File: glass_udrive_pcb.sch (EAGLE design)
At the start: 14 parts, among them IC1 OPA129U, J1 OMNETICS_A75243-001

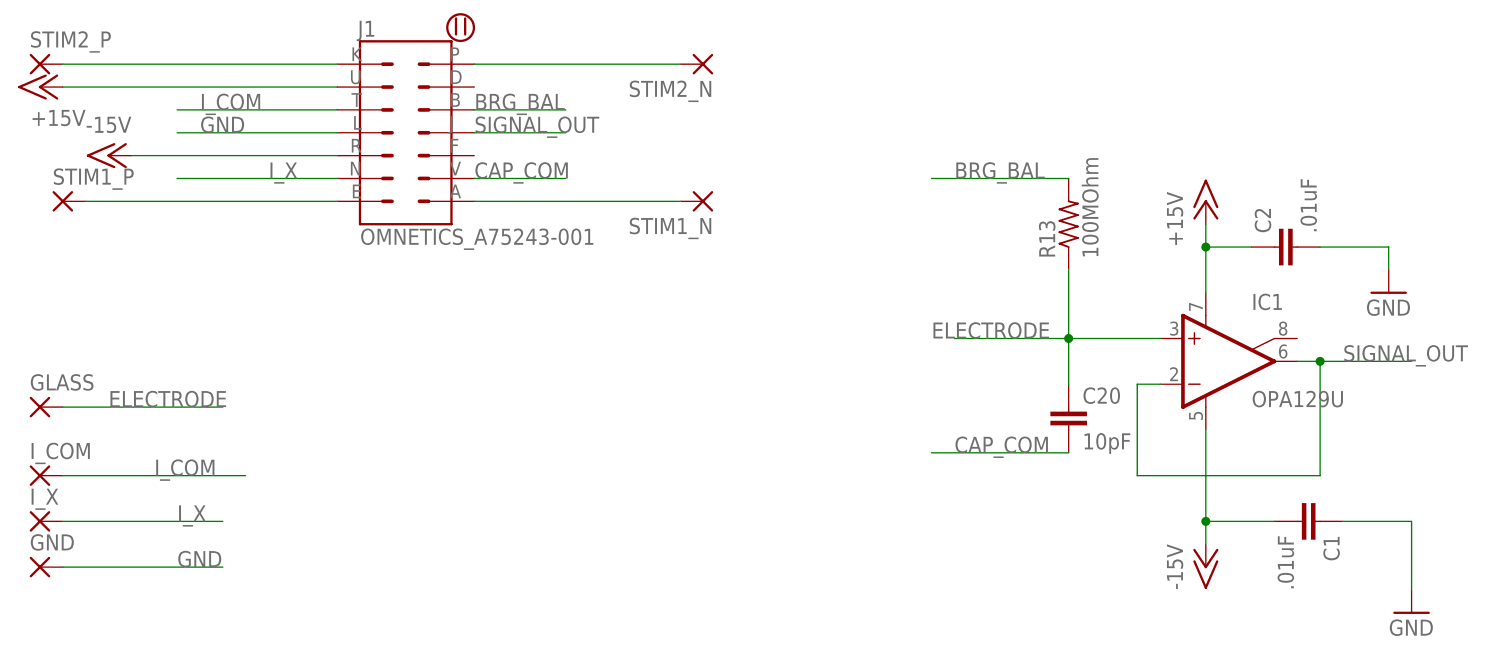
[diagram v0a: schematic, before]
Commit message: smashed labels
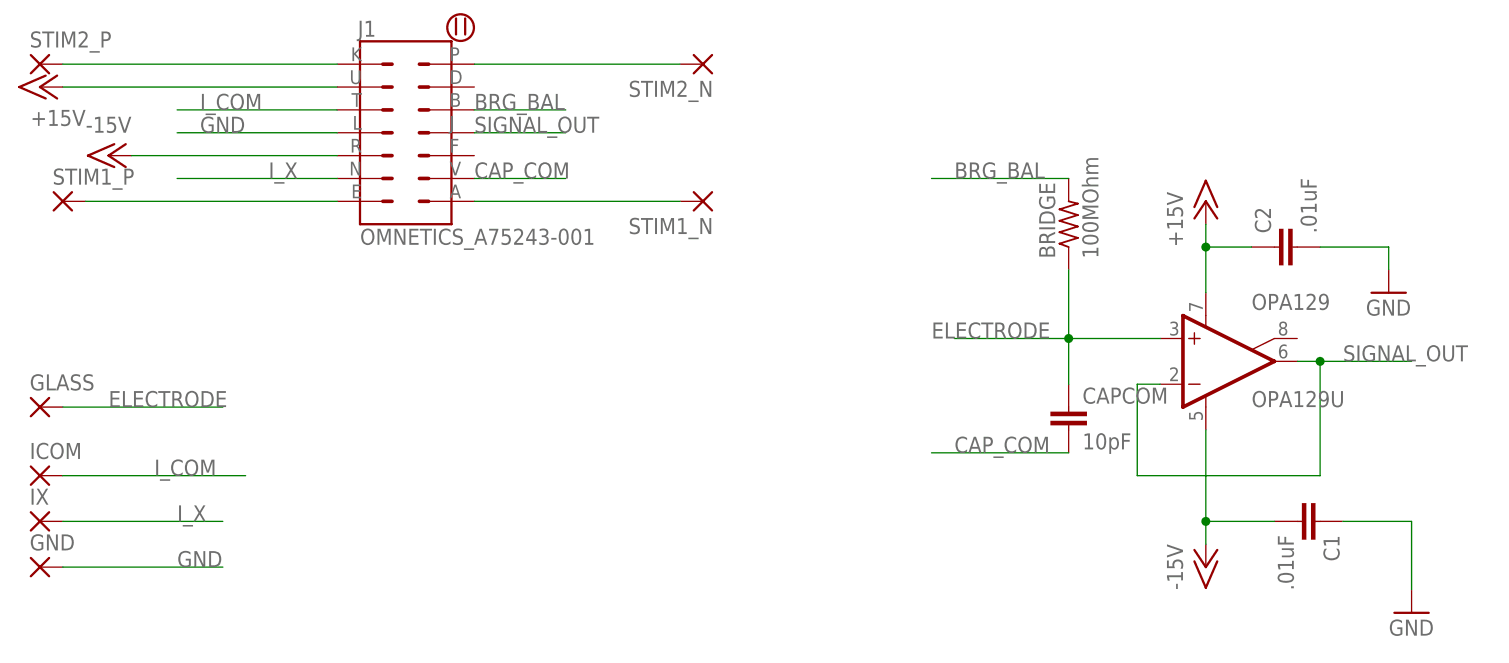
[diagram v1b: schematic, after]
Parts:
- renumbered C20 to CAPCOM, IC1 to OPA129, I_COM to ICOM, I_X to IX, R13 to BRIDGE
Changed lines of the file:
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@@
 </classes>
 <parts>
-<part name="IC1" library="burr-brown" deviceset="OPA129" device="U"/>
+<part name="OPA129" library="burr-brown" deviceset="OPA129" device="U"/>
 <part name="FRAME1" library="frames" deviceset="LETTER_L" device=""/>
 <part name="J1" library="GFL" deviceset="OMNETICS_A75243-001" device=""/>
-<part name="R13" library="GFL" deviceset="R" device="_0402" value="100MOhm"/>
-<part name="C20" library="GFL" deviceset="C" device="_0402" value="10pF"/>
+<part name="BRIDGE" library="GFL" deviceset="R" device="_0402" value="100MOhm"/>
+<part name="CAPCOM" library="GFL" deviceset="C" device="_0402" value="10pF"/>
 <part name="C1" library="GFL" deviceset="C" device="_0402" value=".01uF"/>
 <part name="C2" library="GFL" deviceset="C" device="_0402" value=".01uF"/>
@@
 <part name="GLASS" library="GFL" deviceset="THROUGH-HOLE-30MIL/15MIL" device=""/>
 <part name="STIM2_N" library="GFL" deviceset="THROUGH-HOLE-30MIL/15MIL" device=""/>
-<part name="I_X" library="GFL" deviceset="THROUGH-HOLE-30MIL/15MIL" device=""/>
+<part name="IX" library="GFL" deviceset="THROUGH-HOLE-30MIL/15MIL" device=""/>
 <part name="STIM1_N" library="GFL" deviceset="THROUGH-HOLE-30MIL/15MIL" device=""/>
 <part name="STIM1_P" library="GFL" deviceset="THROUGH-HOLE-30MIL/15MIL" device=""/>
 <part name="STIM2_P" library="GFL" deviceset="THROUGH-HOLE-30MIL/15MIL" device=""/>
-<part name="I_COM" library="GFL" deviceset="THROUGH-HOLE-30MIL/15MIL" device=""/>
+<part name="ICOM" library="GFL" deviceset="THROUGH-HOLE-30MIL/15MIL" device=""/>
 <part name="GND" library="GFL" deviceset="THROUGH-HOLE-30MIL/15MIL" device=""/>
 </parts>
@@
 </plain>
 <instances>
-<instance part="IC1" gate="G$1" x="149.86" y="91.44"/>
+<instance part="OPA129" gate="G$1" x="149.86" y="91.44"/>
 <instance part="FRAME1" gate="G$1" x="-25.4" y="-10.16"/>
 <instance part="FRAME1" gate="G$2" x="121.92" y="-10.16"/>
 <instance part="J1" gate="G$1" x="58.42" y="116.84"/>
-<instance part="R13" gate="R" x="132.08" y="106.68" rot="R90"/>
-<instance part="C20" gate="C" x="132.08" y="86.36"/>
+<instance part="BRIDGE" gate="R" x="132.08" y="106.68" rot="R90"/>
+<instance part="CAPCOM" gate="C" x="132.08" y="86.36"/>
 <instance part="C1" gate="C" x="160.02" y="73.66" rot="R270"/>
 <instance part="C2" gate="C" x="154.94" y="104.14" rot="R90"/>
@@
 <instance part="GLASS" gate="P" x="17.78" y="86.36"/>
 <instance part="STIM2_N" gate="P" x="91.44" y="124.46" rot="R180"/>
-<instance part="I_X" gate="P" x="17.78" y="73.66"/>
+<instance part="IX" gate="P" x="17.78" y="73.66"/>
 <instance part="STIM1_N" gate="P" x="91.44" y="109.22" rot="R180"/>
 <instance part="STIM1_P" gate="P" x="20.32" y="109.22"/>
 <instance part="STIM2_P" gate="P" x="17.78" y="124.46"/>
-<instance part="I_COM" gate="P" x="17.78" y="78.74"/>
+<instance part="ICOM" gate="P" x="17.78" y="78.74"/>
 <instance part="GND" gate="P" x="17.78" y="68.58"/>
 </instances>
@@
 <net name="+15V" class="0">
 <segment>
-<pinref part="IC1" gate="G$1" pin="V+"/>
+<pinref part="OPA129" gate="G$1" pin="V+"/>
 <pinref part="P+1" gate="1" pin="+15V"/>
 <wire x1="147.32" y1="106.68" x2="147.32" y2="104.14" width="0.1524" layer="91"/>
@@
 <net name="-15V" class="0">
 <segment>
-<pinref part="IC1" gate="G$1" pin="V-"/>
+<pinref part="OPA129" gate="G$1" pin="V-"/>
 <pinref part="P-1" gate="1" pin="-15V"/>
 <wire x1="147.32" y1="71.12" x2="147.32" y2="73.66" width="0.1524" layer="91"/>
@@
 <net name="ELECTRODE" class="0">
 <segment>
-<pinref part="IC1" gate="G$1" pin="+IN"/>
+<pinref part="OPA129" gate="G$1" pin="+IN"/>
 <wire x1="142.24" y1="93.98" x2="132.08" y2="93.98" width="0.1524" layer="91"/>
-<pinref part="C20" gate="C" pin="1"/>
+<pinref part="CAPCOM" gate="C" pin="1"/>
 <wire x1="132.08" y1="88.9" x2="132.08" y2="93.98" width="0.1524" layer="91"/>
 <junction x="132.08" y="93.98"/>
-<pinref part="R13" gate="R" pin="1"/>
+<pinref part="BRIDGE" gate="R" pin="1"/>
 <wire x1="132.08" y1="93.98" x2="132.08" y2="101.6" width="0.1524" layer="91"/>
 <wire x1="132.08" y1="93.98" x2="119.38" y2="93.98" width="0.1524" layer="91"/>
@@
 </segment>
 <segment>
-<pinref part="C20" gate="C" pin="2"/>
+<pinref part="CAPCOM" gate="C" pin="2"/>
 <wire x1="132.08" y1="81.28" x2="116.84" y2="81.28" width="0.1524" layer="91"/>
 <label x="119.38" y="81.28" size="1.778" layer="95"/>
@@
 </segment>
 <segment>
-<pinref part="R13" gate="R" pin="2"/>
+<pinref part="BRIDGE" gate="R" pin="2"/>
 <wire x1="132.08" y1="111.76" x2="116.84" y2="111.76" width="0.1524" layer="91"/>
 <label x="119.38" y="111.76" size="1.778" layer="95"/>
@@
 <wire x1="20.32" y1="78.74" x2="40.64" y2="78.74" width="0.1524" layer="91"/>
 <label x="30.48" y="78.74" size="1.778" layer="95"/>
-<pinref part="I_COM" gate="P" pin="P"/>
+<pinref part="ICOM" gate="P" pin="P"/>
 </segment>
 <segment>
@@
 <net name="I_X" class="0">
 <segment>
-<pinref part="I_X" gate="P" pin="P"/>
+<pinref part="IX" gate="P" pin="P"/>
 <wire x1="20.32" y1="73.66" x2="38.1" y2="73.66" width="0.1524" layer="91"/>
 <label x="33.02" y="73.66" size="1.778" layer="95"/>
@@
 </segment>
 <segment>
-<pinref part="IC1" gate="G$1" pin="-IN"/>
+<pinref part="OPA129" gate="G$1" pin="-IN"/>
 <wire x1="142.24" y1="88.9" x2="139.7" y2="88.9" width="0.1524" layer="91"/>
 <wire x1="139.7" y1="88.9" x2="139.7" y2="78.74" width="0.1524" layer="91"/>
 <wire x1="139.7" y1="78.74" x2="160.02" y2="78.74" width="0.1524" layer="91"/>
 <wire x1="160.02" y1="78.74" x2="160.02" y2="91.44" width="0.1524" layer="91"/>
-<pinref part="IC1" gate="G$1" pin="OUT"/>
+<pinref part="OPA129" gate="G$1" pin="OUT"/>
 <wire x1="160.02" y1="91.44" x2="157.48" y2="91.44" width="0.1524" layer="91"/>
 <wire x1="160.02" y1="91.44" x2="170.18" y2="91.44" width="0.1524" layer="91"/>

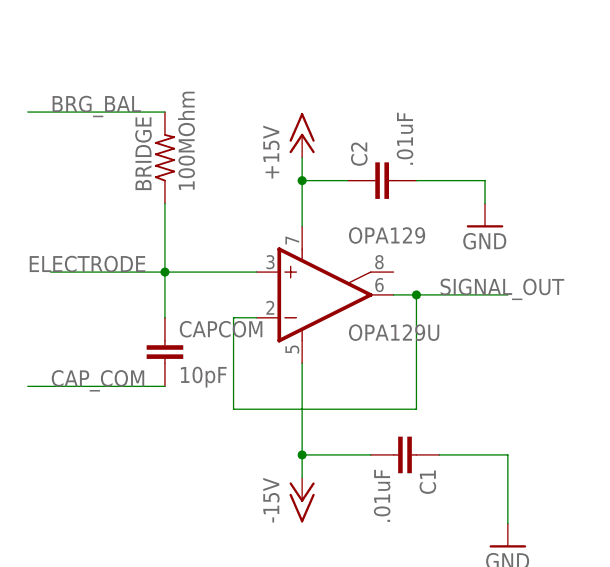
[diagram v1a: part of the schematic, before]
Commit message: Galen's suggested changes to Rev 1.0
I have changed a number of things in your design, one of which is major and the
rest are minor. The major change is that I have added a guard trace to your
design, in accordance with the data sheet for the OPA129. If you are going to
use an ultra-low input bias current op amp, then you should make efforts to
actually achieve the performance that it touts. The other changes are mostly
positioning to accommodate the guard trace, changes to the silk screen on your
board, and simplification of the routing of some traces.

To achieve very low input bias, you need to make sure that there is no leakage
current to the electrode net from the rest of the PCB. There is some parasitic
resistance between neighboring traces in the PCB through the insulator and the
solder-mask. By surrounding the electrode with a copper trace that is driven to
be the same voltage as the electrode, this eliminates parasitic resistance, and
also reduces the stray capacitance of the electrode. I am mainly just following
the recommendations of the data sheet for the OPA129, so for more details see the
data sheet. I moved the bridge resistor and compensation capacitor closer to the
electrode to minimize the length of the electrode trace on your board, since
it's a high impedance trace that should be minimized and protected to avoid
noise pickup. I also placed the cap and res so that the guard trace runs between
the pads. To be honest, with these in place the point of using the OPA129 is
lost on me, since you'll have more parasitic current through these than through
any op amp. However, if you do not place them (which you probably will not need
to), then you will have very little input bias current. Running the trace
through the pads is manufacturable at PCBWay (0.1mm minimum), but may cost more.
I think the difference in cost will be totally worth it. We're not that price
sensitive. I also added a break in the solder mask for the guard traces, once
again to minimize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
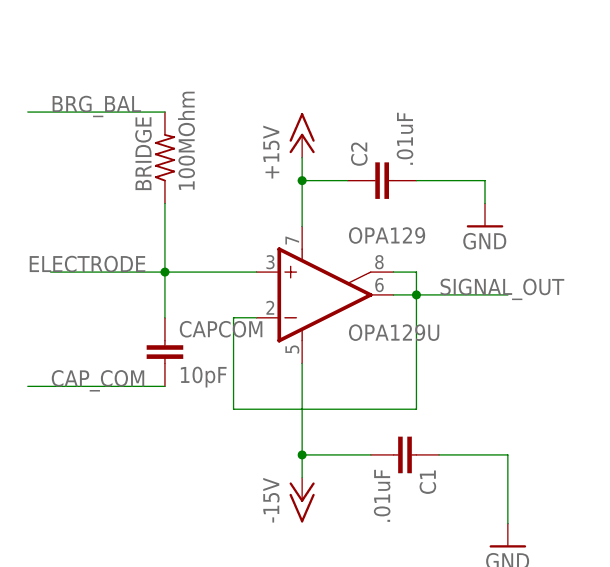
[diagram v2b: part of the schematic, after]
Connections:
- net SIGNAL_OUT: now also OPA129.SUBS
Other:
- note added: "1.0"
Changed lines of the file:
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@@
 <sheet>
 <plain>
+<text x="213.36" y="-2.54" size="1.778" layer="101">1.0</text>
 </plain>
 <instances>
@@
 <junction x="160.02" y="91.44"/>
 <label x="162.56" y="91.44" size="1.778" layer="95"/>
+<pinref part="OPA129" gate="G$1" pin="SUBS"/>
+<wire x1="157.48" y1="93.98" x2="160.02" y2="93.98" width="0.1524" layer="91"/>
+<wire x1="160.02" y1="93.98" x2="160.02" y2="91.44" width="0.1524" layer="91"/>
 </segment>
 </net>
@@
 </sheet>
 </sheets>
+<errors>
+</errors>
 </schematic>
 </drawing>

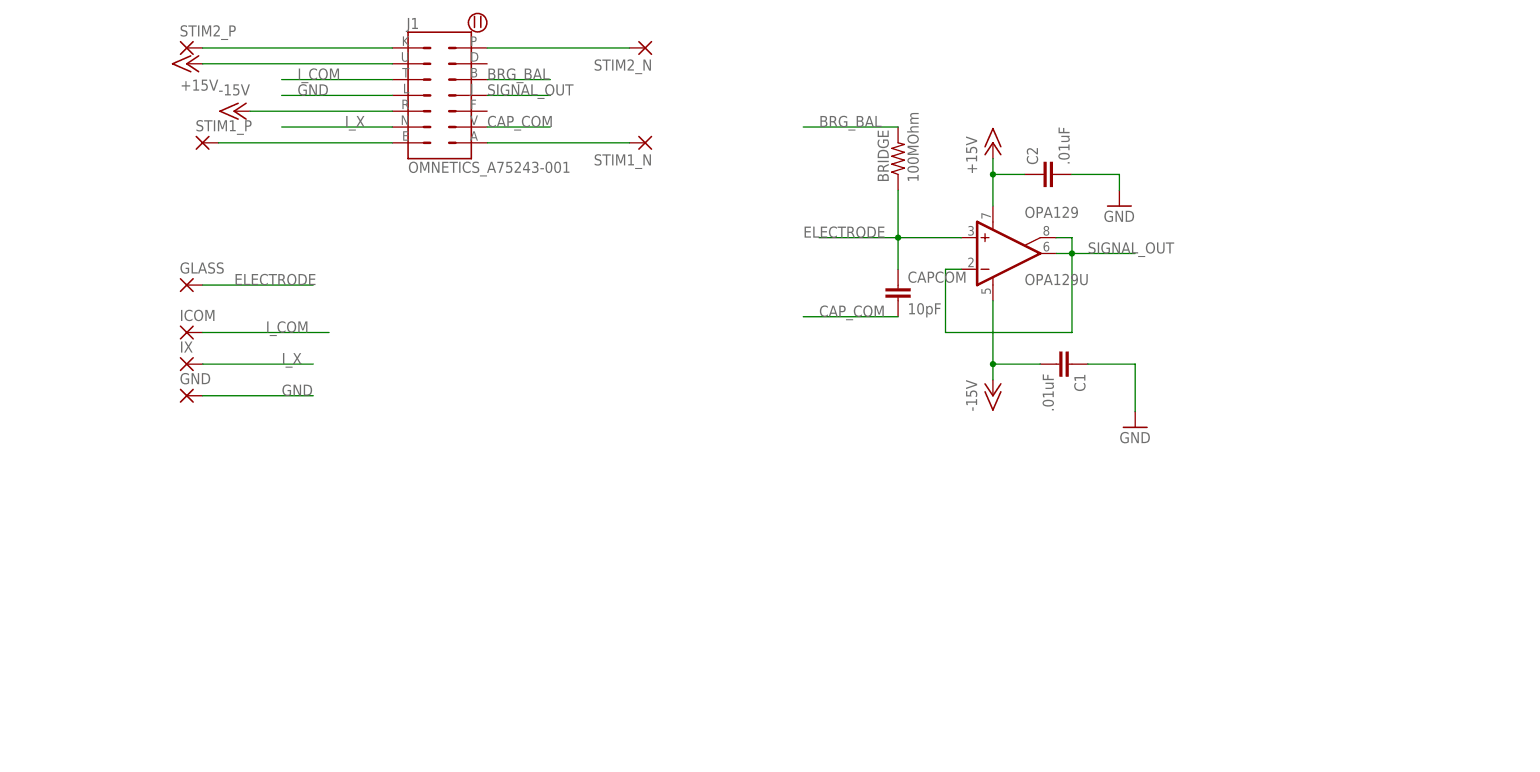
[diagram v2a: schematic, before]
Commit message: Revision AD8224 redesigned to use instrumentation amplifier with a reference electrode. This version has 2 input and 2 INA output channels one for glass electrode and another for a metal electrode.
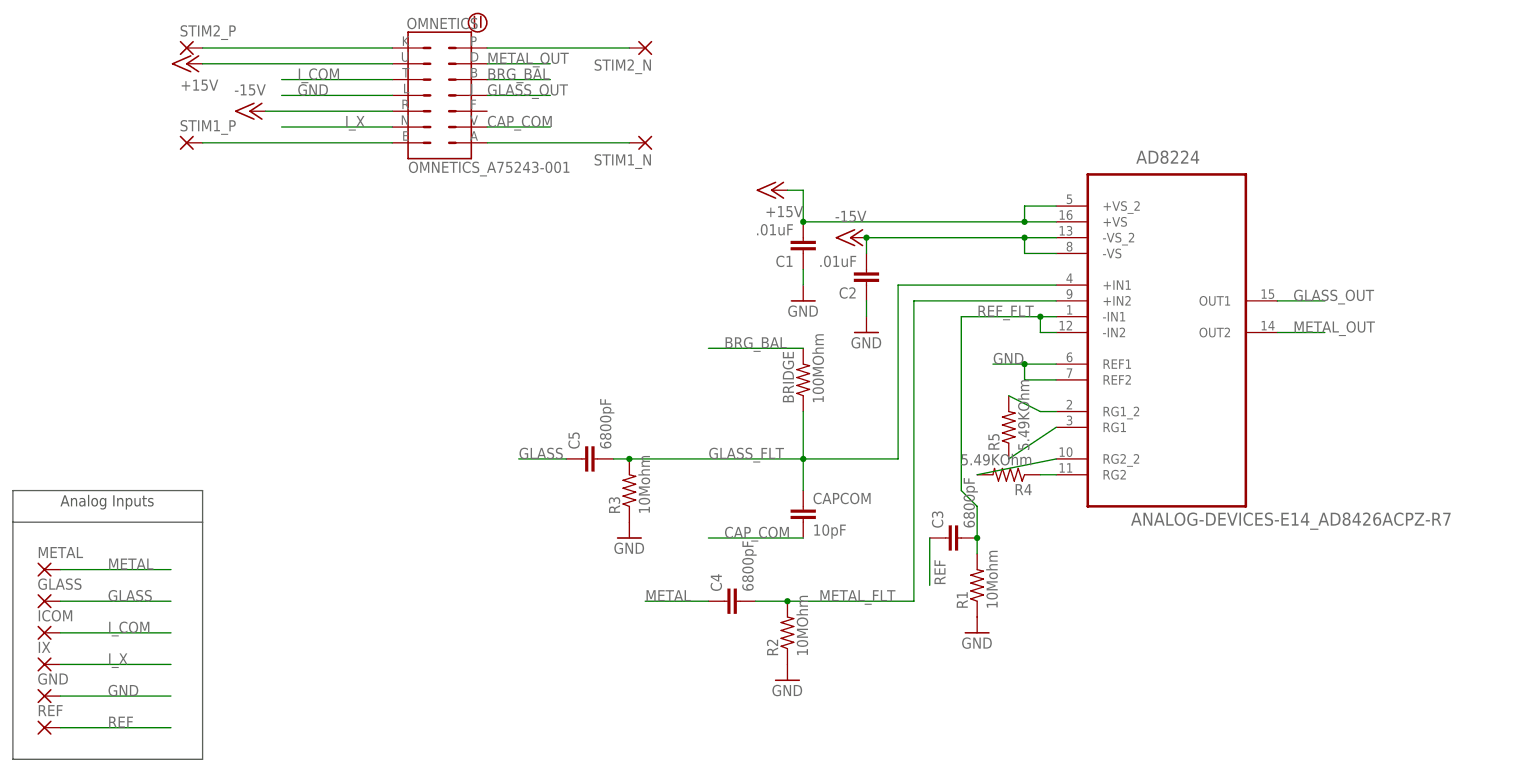
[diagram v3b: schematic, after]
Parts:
- removed OPA129: OPA129U, burr-brown:OPA129U
- added AD8224: ANALOG-DEVICES-E14_AD8426ACPZ-R7, GyroDrive:ANALOG-DEVICES-E14_AD8426ACPZ-R7
- added C3, C4, C5: 6800pF, GFL:C_0201
- added METAL, REF: (no value), GFL:THROUGH-HOLE-30MIL/15MIL
- added R1, R3: 10Mohm, GFL:R_0201
- added R2: 10MOhm, GFL:R_0201
- added R4, R5: 5.49KOhm, GFL:R_0201
- C1, C2: device GFL:C_0402 -> GFL:C_0201
- renumbered J1 to OMNETICS
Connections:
- removed net ELECTRODE: BRIDGE.1, CAPCOM.1, GLASS.P, OPA129.+IN
- removed net SIGNAL_OUT: OMNETICS.J, OPA129.-IN, OPA129.OUT, OPA129.SUBS
- new net GLASS: C5.1, GLASS.P
- new net GLASS_FLT: AD8224.+IN1, BRIDGE.1, C5.2, CAPCOM.1, R3.2
- new net GLASS_OUT: AD8224.OUT1, OMNETICS.J
- new net METAL: C4.1, METAL.P
- new net METAL_FLT: AD8224.+IN2, C4.2, R2.2
- new net METAL_OUT: AD8224.OUT2, OMNETICS.D
- new net N$2: AD8224.RG1_2, R5.2
- new net N$4: AD8224.RG1, R5.1
- new net N$6: AD8224.RG2_2, R4.2
- new net N$8: AD8224.RG2, R4.1
- new net REF: C3.1, REF.P
- new net REF_FLT: AD8224.-IN1, AD8224.-IN2, C3.2, R1.2
- net +15V: now also AD8224.+VS, AD8224.+VS_2, C1.2; no longer C2.1, OPA129.V+
- net -15V: now also AD8224.-VS, AD8224.-VS_2, C2.2; no longer C1.2, OPA129.V-
- net GND: now also AD8224.REF1, AD8224.REF2, C2.1, R1.1, R2.1, R3.1; no longer C2.2
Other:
- note added: "2.0 AD8224"
- note added: "Analog Inputs"
- note removed: "1.0"
- moved on the sheet: BRIDGE, C1, C2, CAPCOM, GLASS, GND, ICOM, IX, STIM1_P
